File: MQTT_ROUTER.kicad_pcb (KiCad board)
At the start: 2 copper layers, 85 x 100 mm, 87 parts, among them J1 Conn_2Rows-07Pins, J2 Conn_02x07_Odd_Even, J3 Screw_Terminal_01x02, J4 Screw_Terminal_01x03, J5 Screw_Terminal_01x03, J6 Screw_Terminal_01x04, J7 Screw_Terminal_01x06, K1 SANYOU_SRD_Form_C, K2 SANYOU_SRD_Form_C, Q1 SS8050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

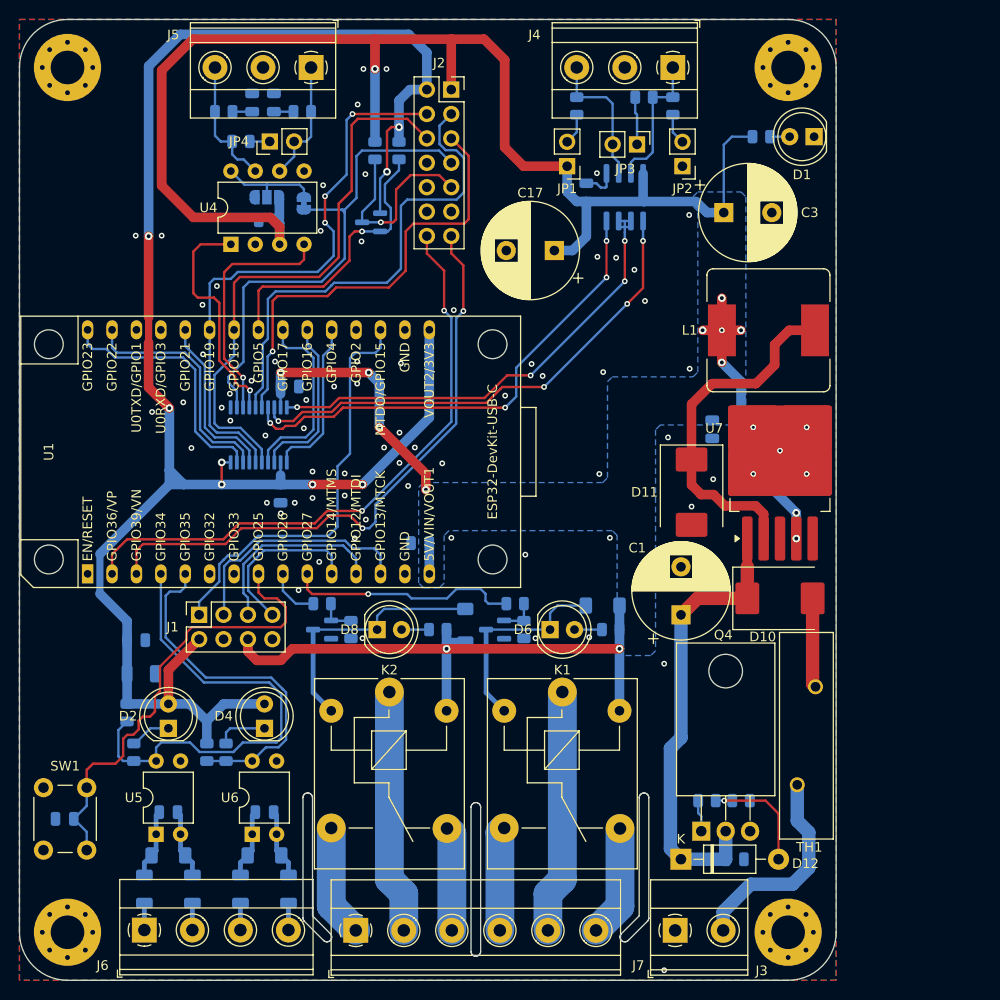
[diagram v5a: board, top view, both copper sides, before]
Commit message: Aumentar mínimo de vía a 0.8/0.4
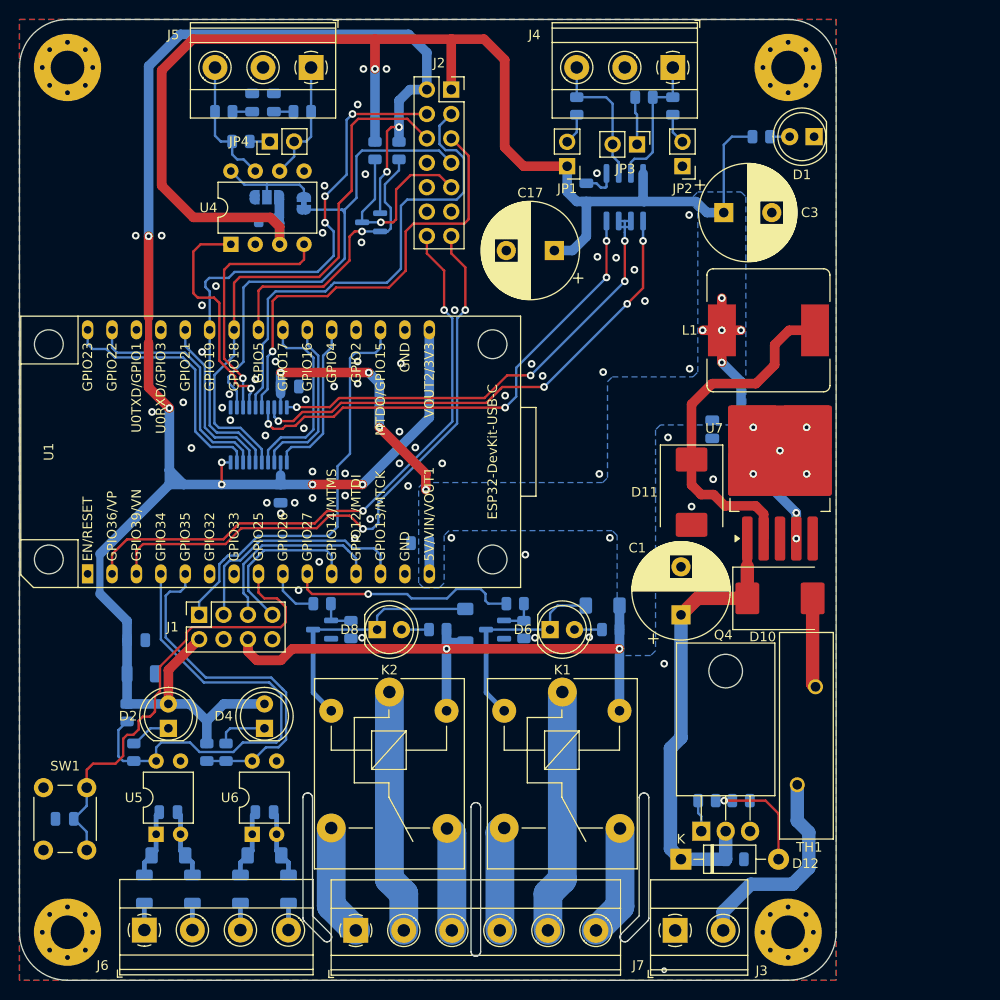
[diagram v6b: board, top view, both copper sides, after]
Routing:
- net /SCL_LO: track 60.1 -> 60.8 mm
- net GND: vias 73 -> 72
